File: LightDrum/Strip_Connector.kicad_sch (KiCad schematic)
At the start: 1 part, among them J601 LED D-SUB

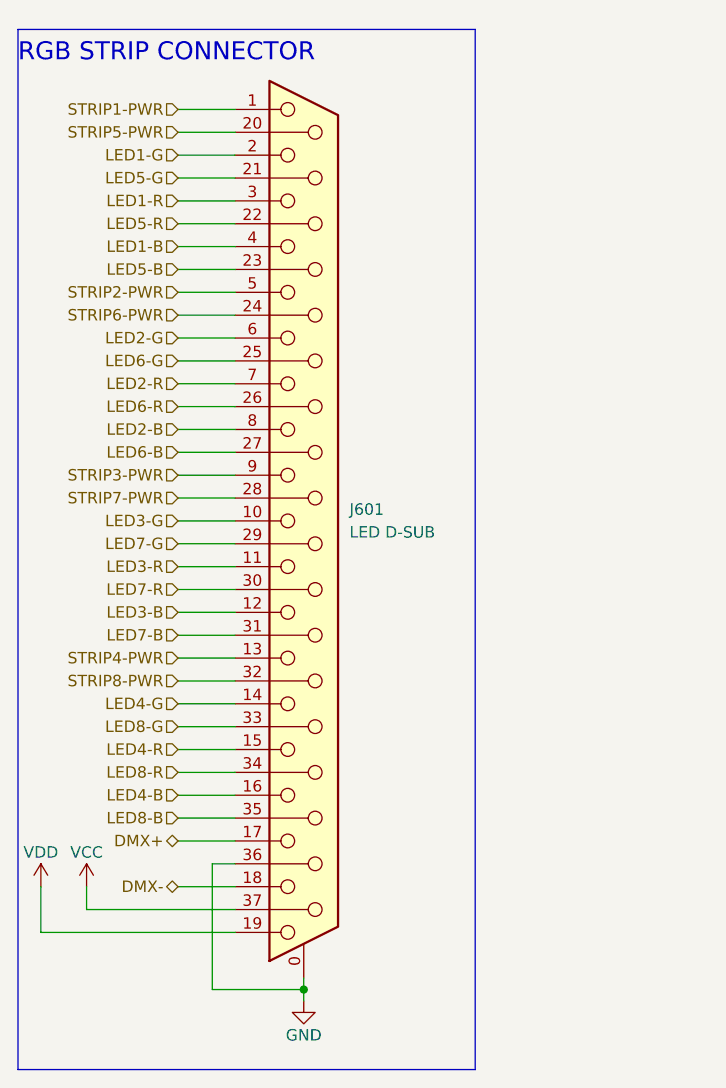
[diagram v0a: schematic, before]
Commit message: Preliminary schematic lock - Starting PCB layout
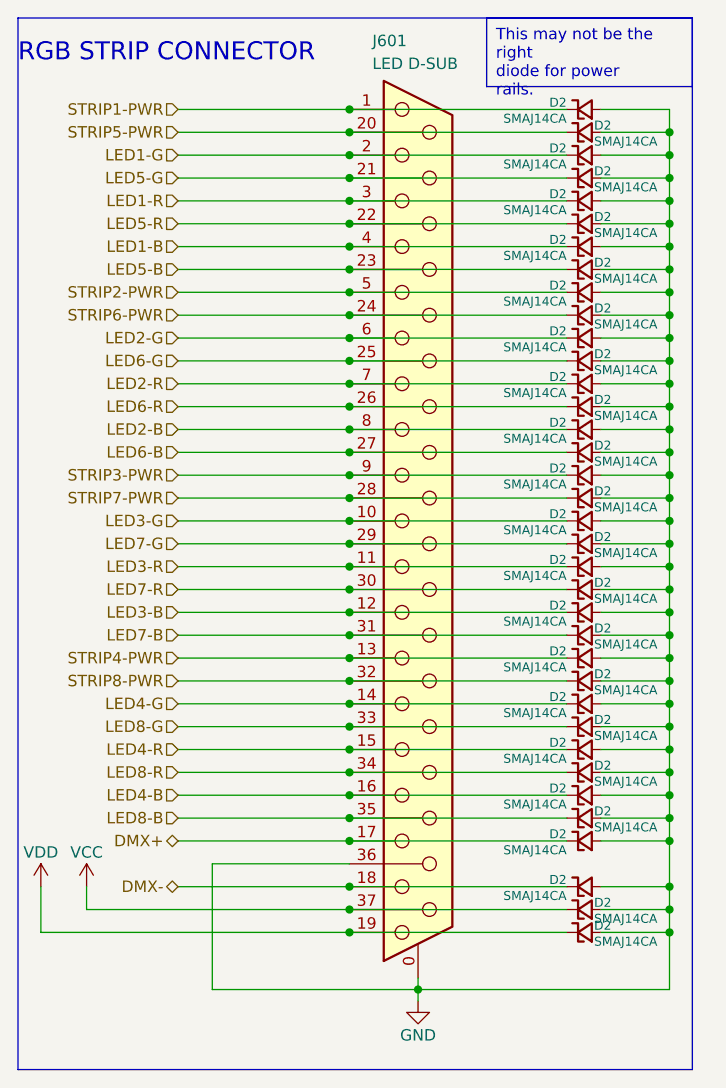
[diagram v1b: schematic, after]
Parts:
- added D2 (x36): SMAJ14CA, Diode_SMD:D_SMA, symbol Daxxn_Device:D_TVS_U
- J601: SupplierPN (none) -> 182-37ME-ND
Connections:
- net DMX+: now also D2.1 (K)
- net DMX-: now also D2.1 (K)
- net GND: now also D2.2 (A), D2.2 (A), D2.2 (A), D2.2 (A), D2.2 (A), D2.2 (A), D2.2 (A), D2.2 (A), D2.2 (A), D2.2 (A), D2.2 (A), D2.2 (A), D2.2 (A), D2.2 (A), D2.2 (A), D2.2 (A), D2.2 (A), D2.2 (A), D2.2 (A), D2.2 (A), D2.2 (A), D2.2 (A), D2.2 (A), D2.2 (A), D2.2 (A), D2.2 (A), D2.2 (A), D2.2 (A), D2.2 (A), D2.2 (A), D2.2 (A), D2.2 (A), D2.2 (A), D2.2 (A), D2.2 (A), D2.2 (A)
- net LED1-B: now also D2.1 (K)
- net LED1-G: now also D2.1 (K)
- net LED1-R: now also D2.1 (K)
- net LED2-B: now also D2.1 (K)
- net LED2-G: now also D2.1 (K)
- net LED2-R: now also D2.1 (K)
- net LED3-B: now also D2.1 (K)
- net LED3-G: now also D2.1 (K)
- net LED3-R: now also D2.1 (K)
- net LED4-B: now also D2.1 (K)
- net LED4-G: now also D2.1 (K)
- net LED4-R: now also D2.1 (K)
- net LED5-B: now also D2.1 (K)
- net LED5-G: now also D2.1 (K)
- net LED5-R: now also D2.1 (K)
- net LED6-B: now also D2.1 (K)
- net LED6-G: now also D2.1 (K)
- net LED6-R: now also D2.1 (K)
- net LED7-B: now also D2.1 (K)
- net LED7-G: now also D2.1 (K)
- net LED7-R: now also D2.1 (K)
- net LED8-B: now also D2.1 (K)
- net LED8-G: now also D2.1 (K)
- net LED8-R: now also D2.1 (K)
- net STRIP1-PWR: now also D2.1 (K)
- net STRIP2-PWR: now also D2.1 (K)
- net STRIP3-PWR: now also D2.1 (K)
- net STRIP4-PWR: now also D2.1 (K)
- net STRIP5-PWR: now also D2.1 (K)
- net STRIP6-PWR: now also D2.1 (K)
- net STRIP7-PWR: now also D2.1 (K)
- net STRIP8-PWR: now also D2.1 (K)
- net VCC: now also D2.1 (K)
- net VDD: now also D2.1 (K)
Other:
- moved on the sheet: J601

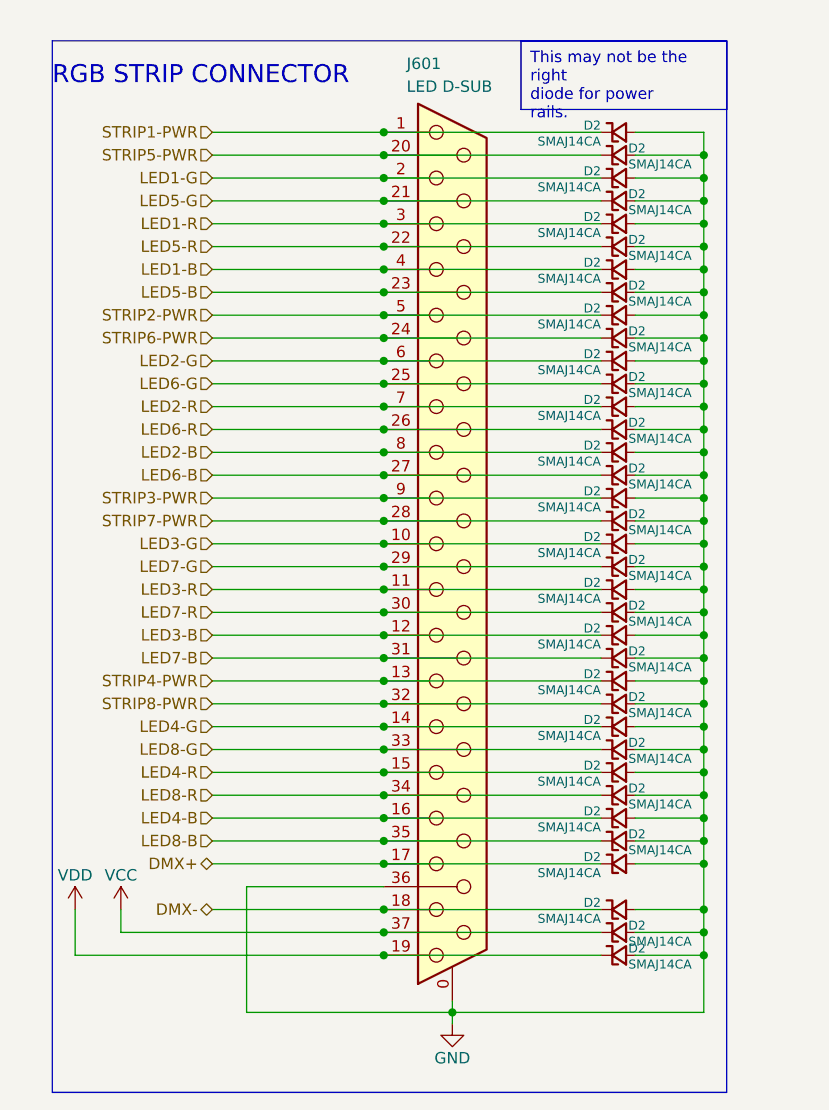
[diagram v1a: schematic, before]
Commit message: Component placement complete
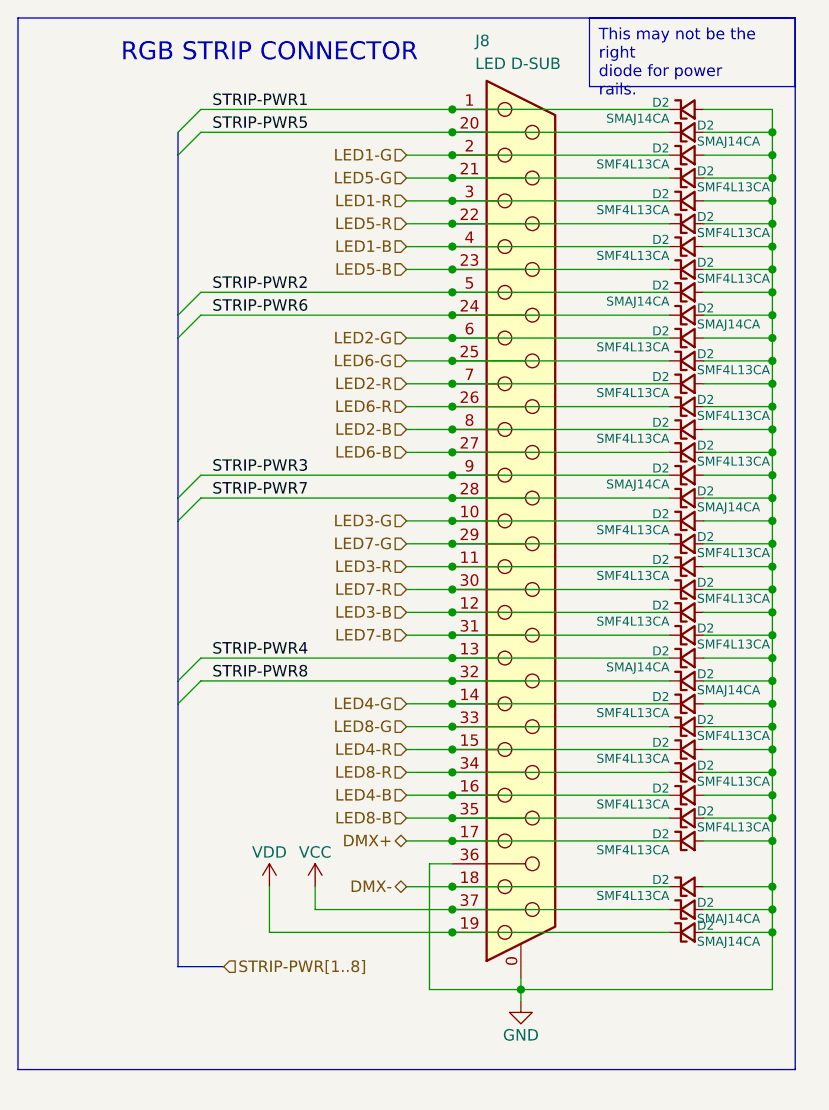
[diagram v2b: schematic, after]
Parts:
- D2: value SMAJ14CA -> SMF4L13CA; footprint Diode_SMD:D_SMA -> Diode_SMD:D_SOD-123F; SupplierPN SMAJ14CA-FDICT-ND -> 18-SMF4L13CACT-ND
- renumbered J601 to J8
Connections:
- net STRIP1-PWR renamed STRIP-PWR1
- net STRIP2-PWR renamed STRIP-PWR2
- net STRIP3-PWR renamed STRIP-PWR3
- net STRIP4-PWR renamed STRIP-PWR4
- net STRIP5-PWR renamed STRIP-PWR5
- net STRIP6-PWR renamed STRIP-PWR6
- net STRIP7-PWR renamed STRIP-PWR7
- net STRIP8-PWR renamed STRIP-PWR8
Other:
- moved on the sheet: D2, J8

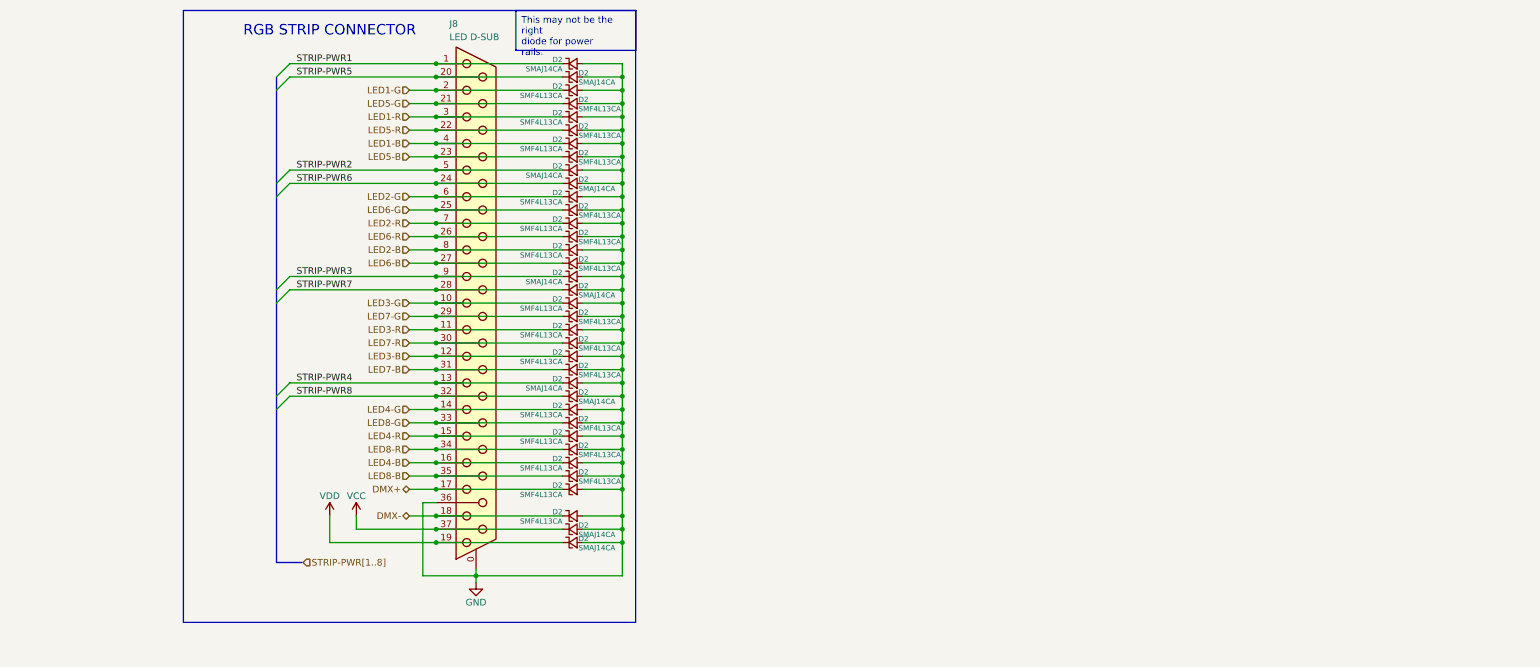
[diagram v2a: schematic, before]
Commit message: Replace DSub with much better ECU conn
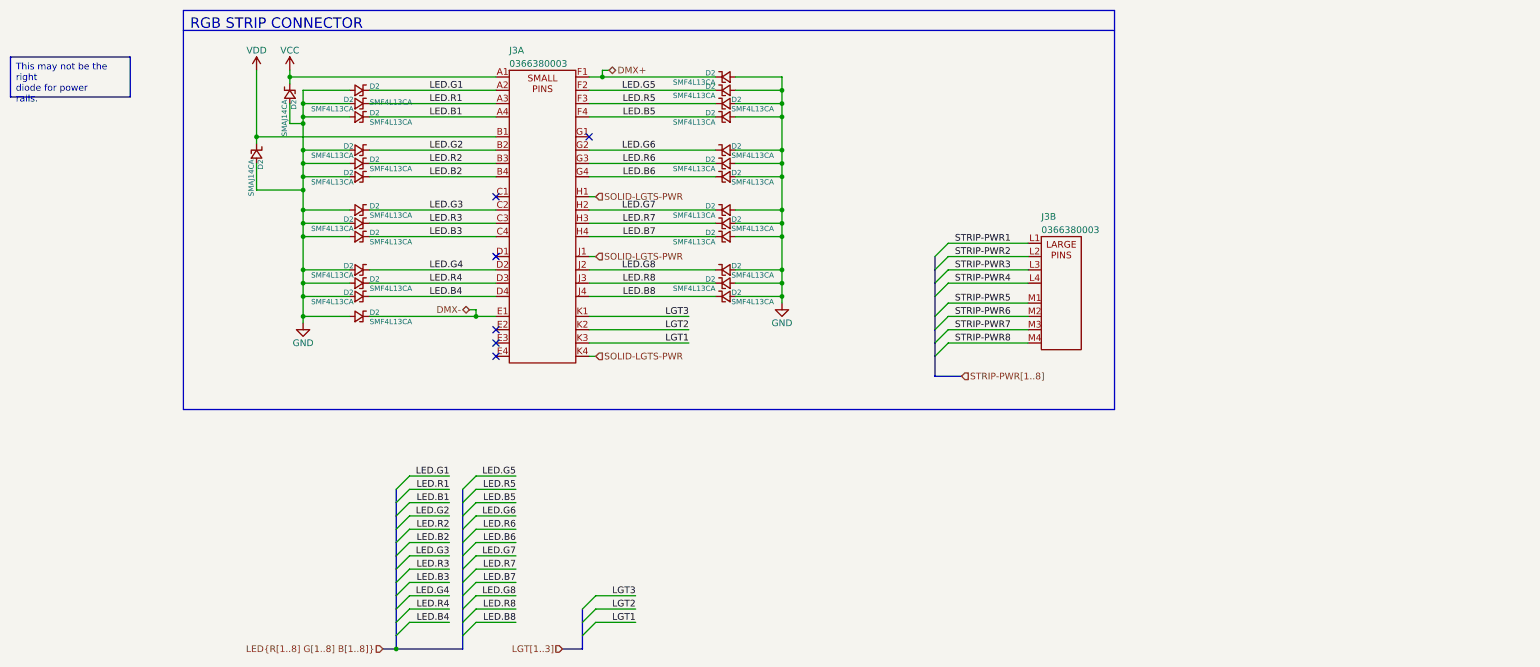
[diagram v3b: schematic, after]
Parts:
- removed D2 (x8): SMAJ14CA, Diode_SMD:D_SMA, symbol Daxxn_Device:D_TVS_U
- removed J8: LED D-SUB, Daxxn_Connectors:DSUB-37-182-037-113R531, symbol Connector:DB37_Female_MountingHoles
- added J3: 0366380003, Daxxn_Connectors:0366380003, symbol Daxxn_Connectors:0366380003
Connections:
- net DMX+: now also D2.1 (K), J3.F1; no longer D2.1 (K)
- net DMX-: now also D2.1 (K), J3.E1; no longer D2.1 (K)
- net STRIP-PWR1: now also J3.L1
- net STRIP-PWR2: now also J3.L2
- net STRIP-PWR3: now also J3.L3
- net STRIP-PWR4: now also J3.L4
- net STRIP-PWR5: now also J3.M1
- net STRIP-PWR6: now also J3.M2
- net STRIP-PWR7: now also J3.M3
- net STRIP-PWR8: now also J3.M4
- net VCC: now also D2.1 (K), J3.A1; no longer D2.1 (K)
- net VDD: now also D2.1 (K), J3.B1; no longer D2.1 (K)
- net LED1-B renamed LED.R6
- net LED.R6: now also J3.G3
- net LED1-G renamed LED.G5
- net LED.G5: now also J3.F2
- net LED1-R renamed LED.B5
- net LED.B5: now also J3.F4
- net LED2-B renamed LED.R8
- net LED.R8: now also J3.J3
- net LED2-G renamed LED.G7
- net LED.G7: now also J3.H2
- net LED2-R renamed LED.B7
- net LED.B7: now also J3.H4
- net LED3-B renamed LED.R2
- net LED.R2: now also J3.B3
- net LED3-G renamed LED.G1
- net LED.G1: now also J3.A2
- net LED3-R renamed LED.B1
- net LED.B1: now also J3.A4
- net LED4-B renamed LED.R4
- net LED.R4: now also J3.D3
- net LED4-G renamed LED.G3
- net LED.G3: now also J3.C2
- net LED4-R renamed LED.B3
- net LED.B3: now also J3.C4
- net LED5-B renamed LED.B6
- net LED.B6: now also J3.G4
- net LED5-G renamed LED.R5
- net LED.R5: now also J3.F3
- net LED5-R renamed LED.G6
- net LED.G6: now also J3.G2
- net LED6-B renamed LED.B8
- net LED.B8: now also J3.J4
- net LED6-G renamed LED.R7
- net LED.R7: now also J3.H3
- net LED6-R renamed LED.G8
- net LED.G8: now also J3.J2
- net LED7-B renamed LED.B2
- net LED.B2: now also J3.B4
- net LED7-G renamed LED.R1
- net LED.R1: now also J3.A3
- net LED7-R renamed LED.G2
- net LED.G2: now also J3.B2
- net LED8-B renamed LED.B4
- net LED.B4: now also J3.D4
- net LED8-G renamed LED.R3
- net LED.R3: now also J3.C3
- net LED8-R renamed LED.G4
- net LED.G4: now also J3.D2
- new net LGT1: J3.K3
- new net LGT2: J3.K2
- new net LGT3: J3.K1
- new net SOLID-LGTS-PWR: J3.H1, J3.J1, J3.K4
- no-connect marks 0 -> 6
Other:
- moved on the sheet: D2

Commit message: Organize old files and generate interface gerbers
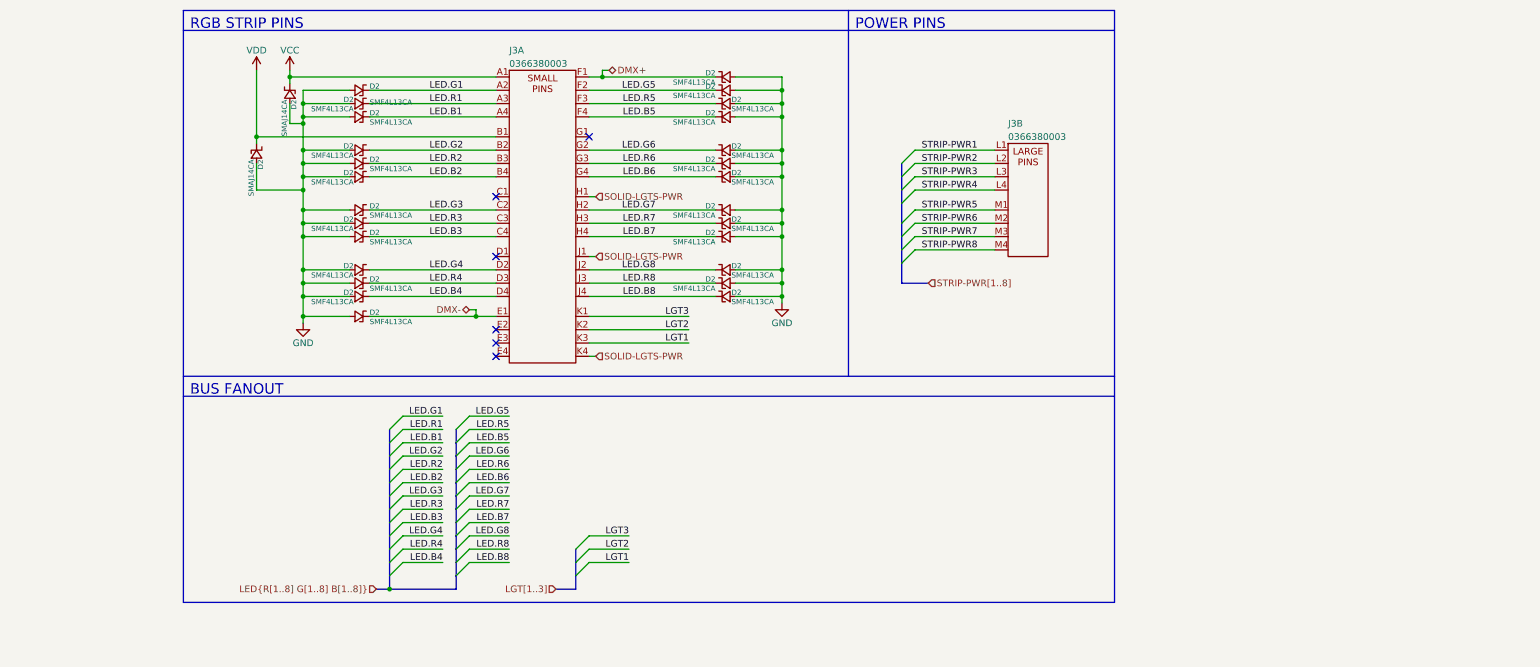
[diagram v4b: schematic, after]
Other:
- note added: "BUS FANOUT"
- note added: "POWER PINS"
- note added: "RGB STRIP PINS"
- note removed: "RGB STRIP CONNECTOR"
- moved on the sheet: J3B

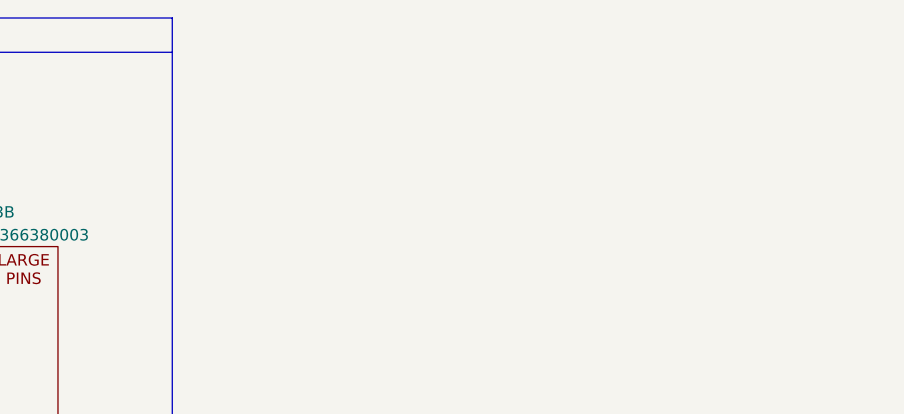
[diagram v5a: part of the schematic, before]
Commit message: fix screen ctrl bugs and add I2S data transfer
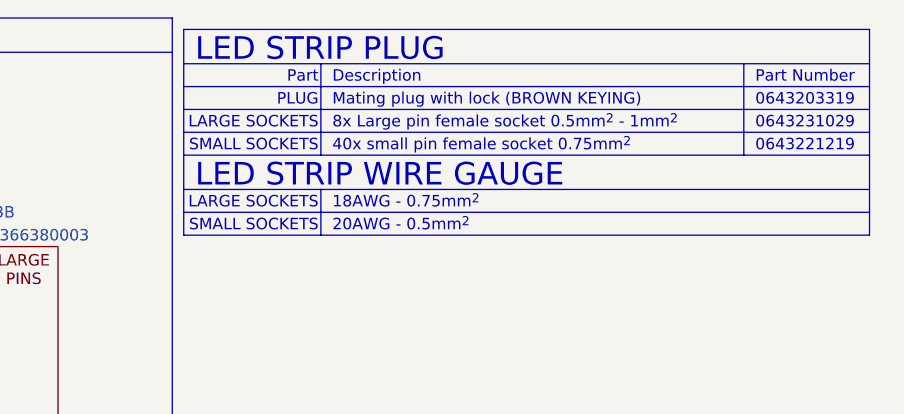
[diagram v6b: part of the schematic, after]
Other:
- note added: "0643203319"
- note added: "0643221219"
- note added: "0643231029"
- note added: "18AWG - 0.75mm^{2}"
- note added: "20AWG - 0.5mm^{2}"
- note added: "40x small pin female socket 0.75mm^{2}"
- note added: "8x Large pin female socket 0.5mm^{2} - 1mm^{2}"
- note added: "Description"
- note added: "LARGE SOCKETS"
- note added: "LED STRIP PLUG"
- note added: "LED STRIP WIRE GAUGE"
- note added: "Mating plug with lock (BROWN KEYING)"
- note added: "PLUG"
- note added: "Part"
- note added: "Part Number"
- note added: "SMALL SOCKETS"

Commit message: REV13 - Update to KiCAD 8
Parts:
- renumbered D2 to D10, D2 to D11, D2 to D12, D2 to D13, D2 to D14, D2 to D15, D2 to D18, D2 to D19, D2 to D20, D2 to D21, D2 to D22, D2 to D23, D2 to D26, D2 to D27, D2 to D28, D2 to D29, D2 to D30, D2 to D31, D2 to D34, D2 to D35, D2 to D36, D2 to D37, D2 to D38, D2 to D39, D2 to D40, D2 to D41, D2 to D42, D2 to D43

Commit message: REV13 - Revert to KiCAD 7
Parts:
- renumbered D30 to D2, D14 to D2, D23 to D2, D18 to D2, D22 to D2, D19 to D2, D10 to D2, D37 to D2, D38 to D2, D26 to D2, D40 to D2, D42 to D2, D29 to D2, D27 to D2, D20 to D2, D15 to D2, D34 to D2, D35 to D2, D28 to D2, D39 to D2, D43 to D2, D36 to D2, D13 to D2, D12 to D2, D41 to D2, D31 to D2, D11 to D2, D21 to D2
